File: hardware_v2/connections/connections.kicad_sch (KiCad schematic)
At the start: 8 parts, among them SW1 Encoder, SW2 PTT Button, SW3 Power switch

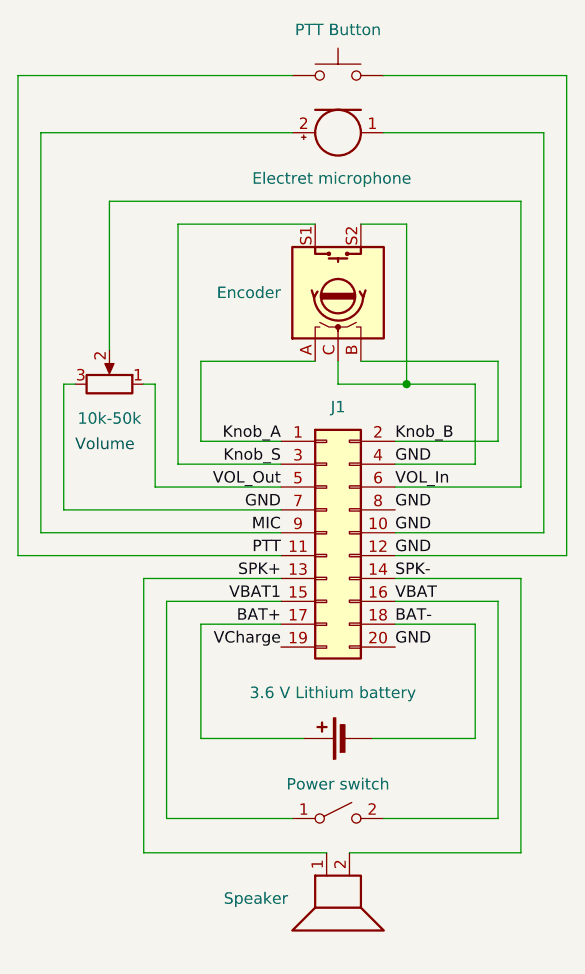
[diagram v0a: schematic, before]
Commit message: Make wiring diagram more clear
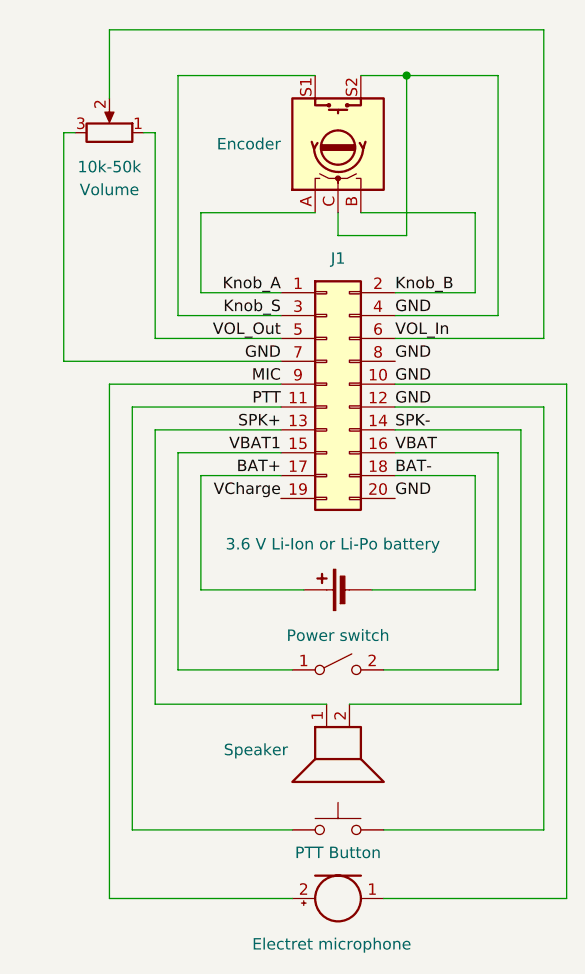
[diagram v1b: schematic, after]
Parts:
- BT1: value 3.6 V Lithium battery -> 3.6 V Li-Ion or Li-Po battery
- RV1: Comment (none) -> Volume
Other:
- note removed: "Volume"
- moved on the sheet: J1
